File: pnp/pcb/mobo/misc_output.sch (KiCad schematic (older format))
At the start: 45 parts, among them J10 MF3, J11 MF4, J12 DOWNWARDS_LIGHT, J13 UPWARDS_LIGHT, J14 5V_INJECTION, J16 RS-485_2, J17 RS-485_3, J21 AUX1, J22 AUX2, J23 QWIIC1, J24 QWIIC2, J25 RS-485_1, J6 SERVO1, J7 SERVO2, J8 MF1, J9 MF2, Q1 IRF540N, Q2 IRF540N, Q3 IRF540N, Q4 IRF540N, U15 TC4424A, U16 TC4424A, U2 SP3485EN, U3 SP3485EN, U4 SP3485EN

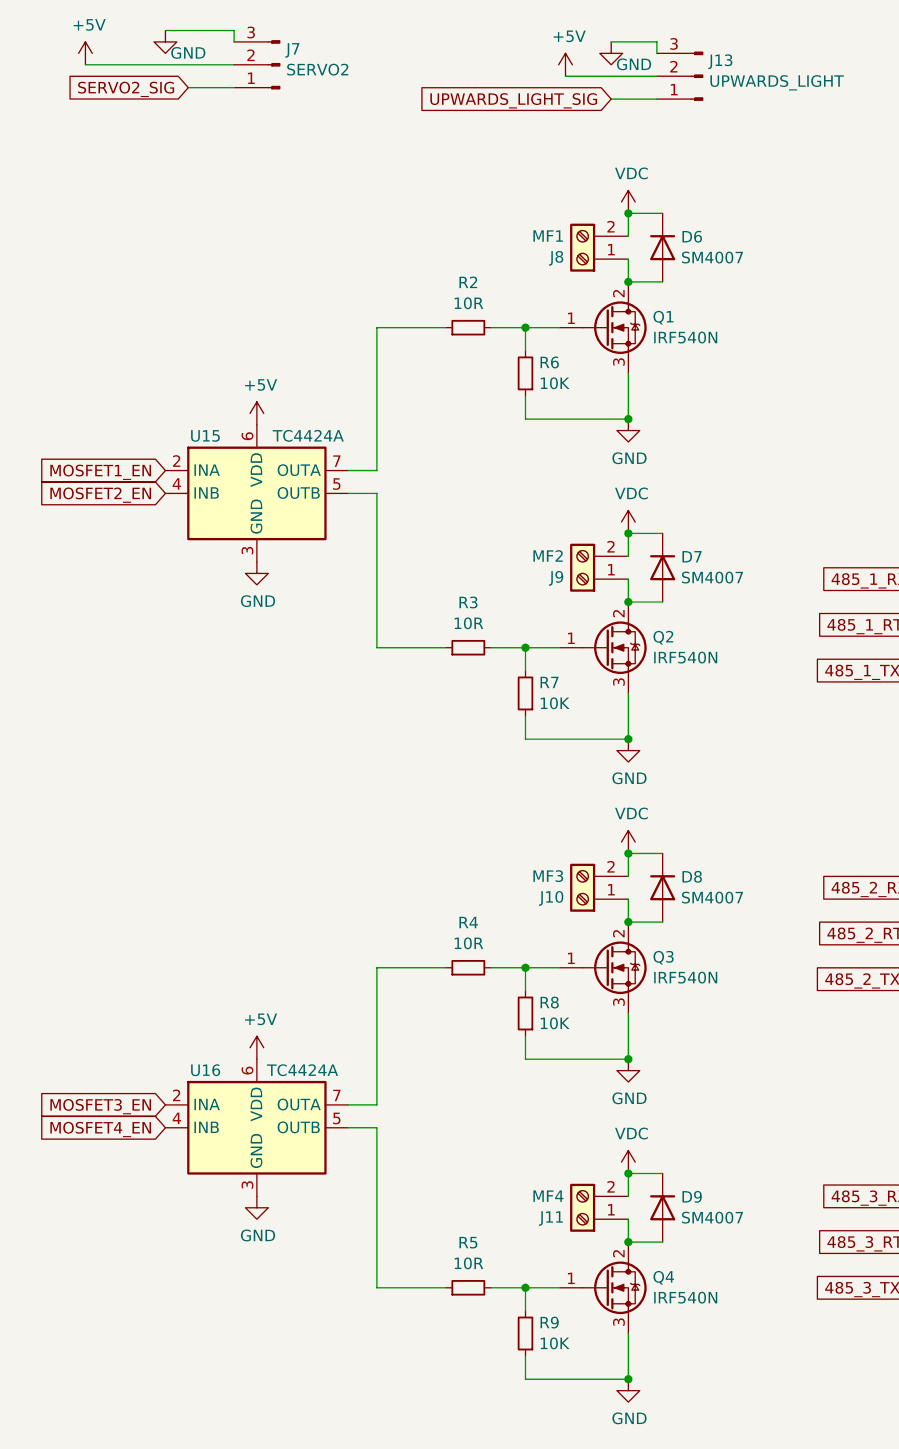
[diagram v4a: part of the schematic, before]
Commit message: Revert 24V support, only routing is left
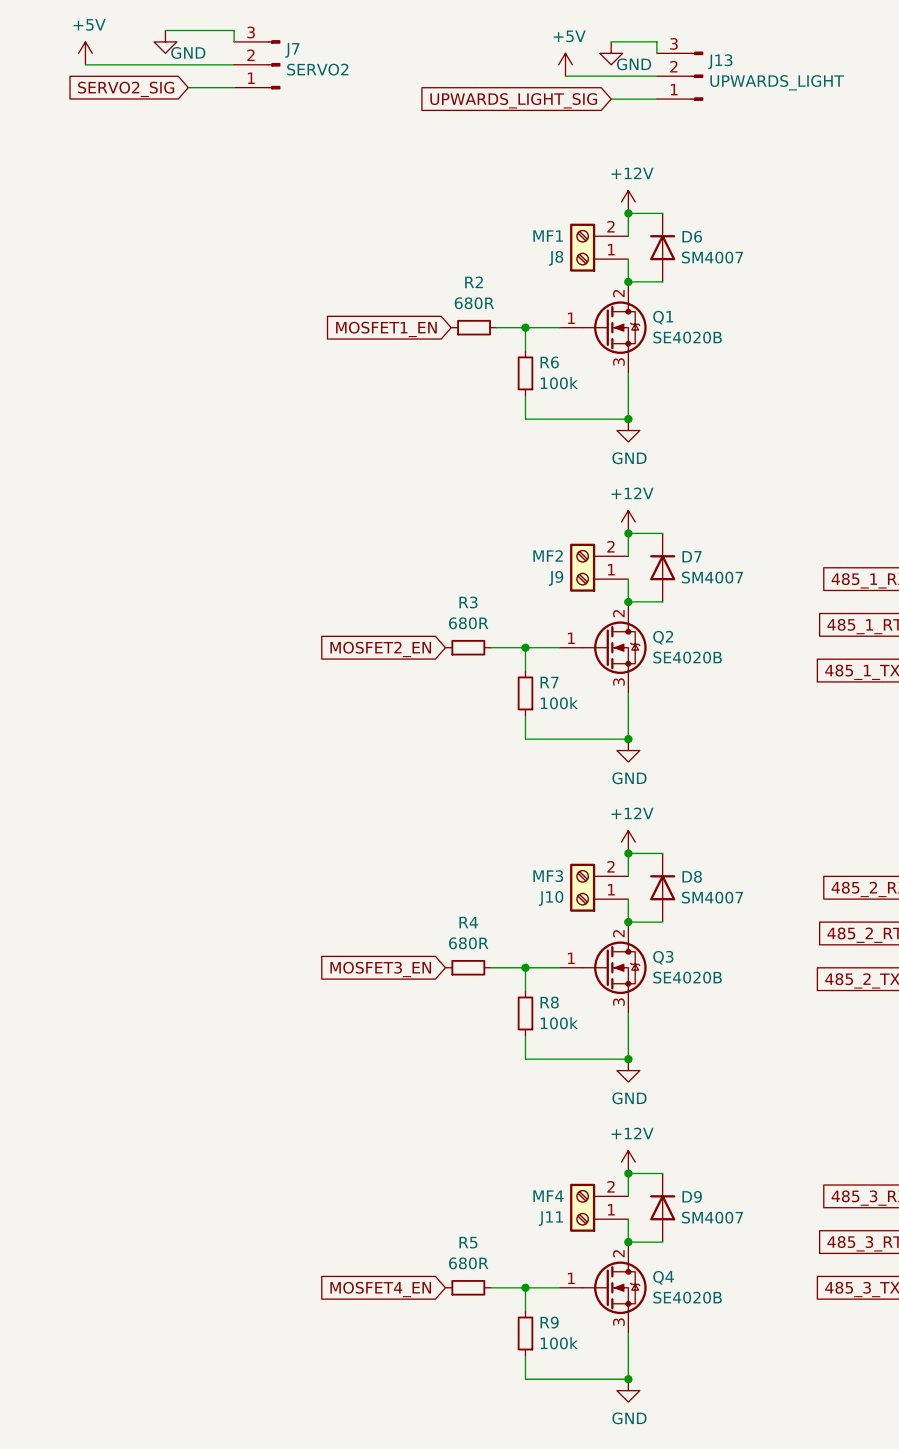
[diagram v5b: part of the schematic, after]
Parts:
- removed Q1, Q2, Q3, Q4: IRF540N, Package_TO_SOT_SMD:TO-252-2, symbol Transistor_FET:IRF540N
- removed U15, U16: TC4424A, Package_SO:SOIC-8_3.9x4.9mm_P1.27mm, symbol index:TC4424A
- added Q1, Q2, Q3, Q4: SE4020B, Package_TO_SOT_SMD:TO-252-2, symbol index:SE4020B
- R2, R3, R4, R5: value 10R -> 680R
- R6, R7, R8, R9: value 10K -> 100k
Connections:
- net GND: now also Q1.3 (S), Q2.3 (S), Q3.3 (S), Q4.3 (S)
- net MOSFET1_EN: now also R2.1
- net MOSFET2_EN: now also R3.1
- net MOSFET3_EN: now also R4.1
- net MOSFET4_EN: now also R5.1
- net at R2.2, R6.2: now also Q1.1 (G)
- net at D6.2 (A), J8.1 (Pin_1): now also Q1.2 (D)
- net at R3.2, R7.2: now also Q2.1 (G)
- net at D7.2 (A), J9.1 (Pin_1): now also Q2.2 (D)
- net at R4.2, R8.2: now also Q3.1 (G)
- net at D8.2 (A), J10.1 (Pin_1): now also Q3.2 (D)
- net at R5.2, R9.2: now also Q4.1 (G)
- net at D9.2 (A), J11.1 (Pin_1): now also Q4.2 (D)
- net VDC renamed +12V
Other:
- moved on the sheet: R2

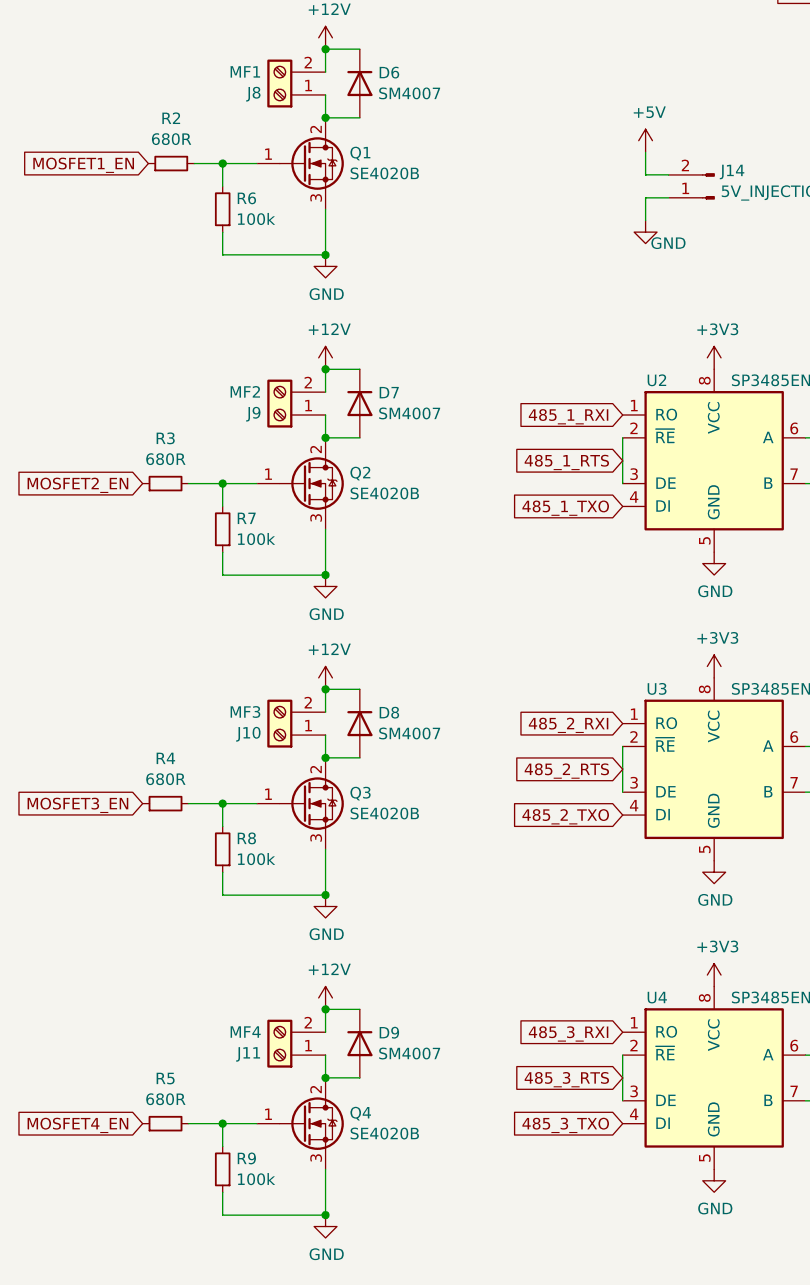
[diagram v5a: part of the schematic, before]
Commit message: Replaced MOSFET with TSM900
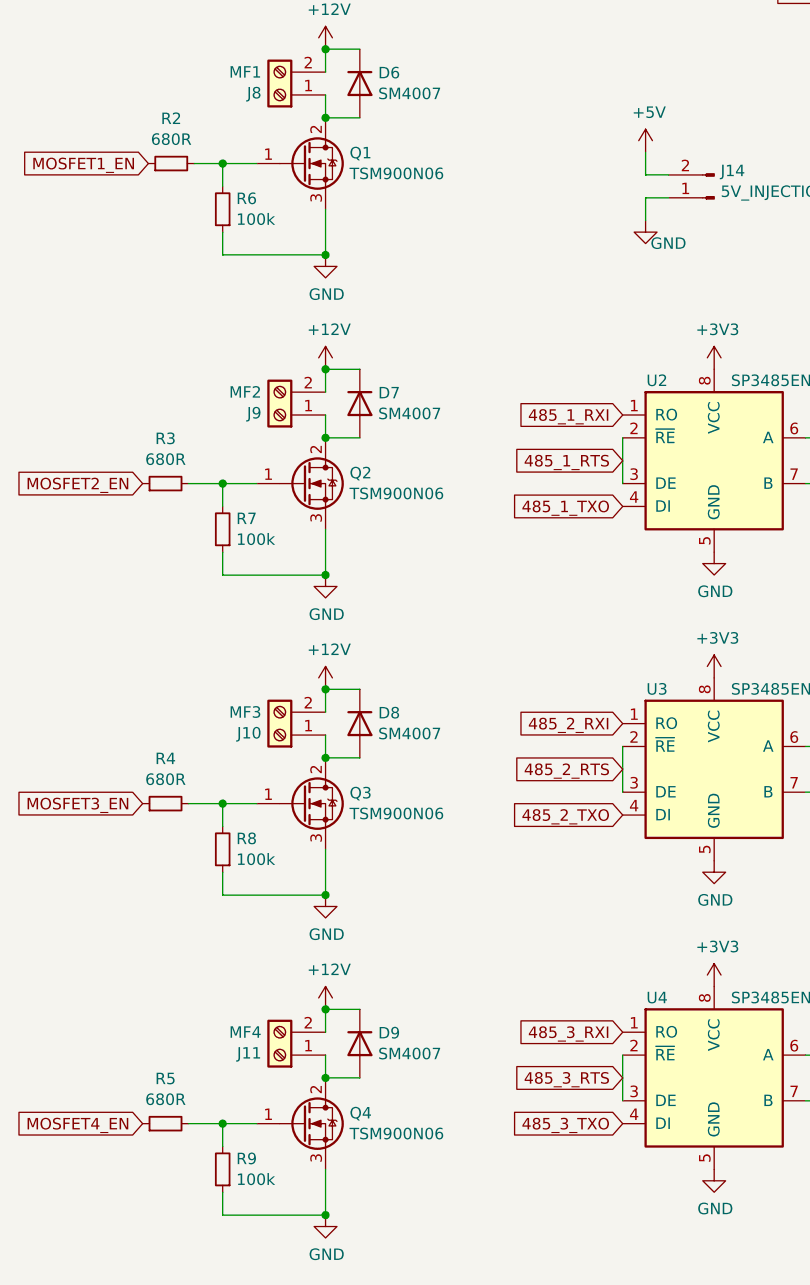
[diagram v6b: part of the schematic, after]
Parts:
- removed Q1, Q2, Q3, Q4: SE4020B, Package_TO_SOT_SMD:TO-252-2, symbol index:SE4020B
- added Q1, Q2, Q3, Q4: TSM900N06, Package_TO_SOT_SMD:TO-252-2, symbol index:TSM900N06
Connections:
- net GND: now also Q1.3 (S), Q2.3 (S), Q3.3 (S), Q4.3 (S)
- net at R2.2, R6.2: now also Q1.1 (G)
- net at D6.2 (A), J8.1 (Pin_1): now also Q1.2 (D)
- net at R3.2, R7.2: now also Q2.1 (G)
- net at D7.2 (A), J9.1 (Pin_1): now also Q2.2 (D)
- net at R4.2, R8.2: now also Q3.1 (G)
- net at D8.2 (A), J10.1 (Pin_1): now also Q3.2 (D)
- net at R5.2, R9.2: now also Q4.1 (G)
- net at D9.2 (A), J11.1 (Pin_1): now also Q4.2 (D)
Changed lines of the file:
@@
 Wire Wire Line
 	2875 2650 3025 2650
-$Comp
-L index:SE4020B Q1
-U 1 1 5FEBE1D6
-P 3225 2650
-F 0 "Q1" H 3430 2696 50  0000 L CNN
-F 1 "SE4020B" H 3430 2605 50  0000 L CNN
-F 2 "Package_TO_SOT_SMD:TO-252-2" H 3475 2575 50  0001 L CIN
-F 3 "https://datasheet.lcsc.com/szlcsc/1912111437_SINO-IC-SE4020B_C396085.pdf" H 3225 2650 50  0001 L CNN
-	1    3225 2650
-	1    0    0    -1
-$EndComp
-Connection ~ 3325 2450
-$Comp
-L index:SE4020B Q2
-U 1 1 5FEC32EF
-P 3225 4050
-F 0 "Q2" H 3430 4096 50  0000 L CNN
-F 1 "SE4020B" H 3430 4005 50  0000 L CNN
-F 2 "Package_TO_SOT_SMD:TO-252-2" H 3475 3975 50  0001 L CIN
-F 3 "https://datasheet.lcsc.com/szlcsc/1912111437_SINO-IC-SE4020B_C396085.pdf" H 3225 4050 50  0001 L CNN
-	1    3225 4050
-	1    0    0    -1
-$EndComp
-Connection ~ 3325 3850
-$Comp
-L index:SE4020B Q3
-U 1 1 5FEC4E58
-P 3225 5450
-F 0 "Q3" H 3430 5496 50  0000 L CNN
-F 1 "SE4020B" H 3430 5405 50  0000 L CNN
-F 2 "Package_TO_SOT_SMD:TO-252-2" H 3475 5375 50  0001 L CIN
-F 3 "https://datasheet.lcsc.com/szlcsc/1912111437_SINO-IC-SE4020B_C396085.pdf" H 3225 5450 50  0001 L CNN
-	1    3225 5450
-	1    0    0    -1
-$EndComp
-Connection ~ 3325 5250
-$Comp
-L index:SE4020B Q4
-U 1 1 5FEC7D03
-P 3225 6850
-F 0 "Q4" H 3430 6896 50  0000 L CNN
-F 1 "SE4020B" H 3430 6805 50  0000 L CNN
-F 2 "Package_TO_SOT_SMD:TO-252-2" H 3475 6775 50  0001 L CIN
-F 3 "https://datasheet.lcsc.com/szlcsc/1912111437_SINO-IC-SE4020B_C396085.pdf" H 3225 6850 50  0001 L CNN
-	1    3225 6850
-	1    0    0    -1
-$EndComp
-Connection ~ 3325 6650
 Wire Wire Line
 	3475 2150 3325 2150
@@
 $EndComp
 Connection ~ 3325 6350
+$Comp
+L index:TSM900N06 Q1
+U 1 1 5FE4F23E
+P 3225 2650
+F 0 "Q1" H 3430 2696 50  0000 L CNN
+F 1 "TSM900N06" H 3430 2605 50  0000 L CNN
+F 2 "Package_TO_SOT_SMD:TO-252-2" H 3475 2575 50  0001 L CIN
+F 3 "https://datasheet.lcsc.com/szlcsc/1912111437_SINO-IC-SE4020B_C396085.pdf" H 3225 2650 50  0001 L CNN
+	1    3225 2650
+	1    0    0    -1
+$EndComp
+Connection ~ 3325 2450
+$Comp
+L index:TSM900N06 Q2
+U 1 1 5FE667F0
+P 3225 4050
+F 0 "Q2" H 3430 4096 50  0000 L CNN
+F 1 "TSM900N06" H 3430 4005 50  0000 L CNN
+F 2 "Package_TO_SOT_SMD:TO-252-2" H 3475 3975 50  0001 L CIN
+F 3 "https://datasheet.lcsc.com/szlcsc/1912111437_SINO-IC-SE4020B_C396085.pdf" H 3225 4050 50  0001 L CNN
+	1    3225 4050
+	1    0    0    -1
+$EndComp
+Connection ~ 3325 3850
+$Comp
+L index:TSM900N06 Q3
+U 1 1 5FE6BC8C
+P 3225 5450
+F 0 "Q3" H 3430 5496 50  0000 L CNN
+F 1 "TSM900N06" H 3430 5405 50  0000 L CNN
+F 2 "Package_TO_SOT_SMD:TO-252-2" H 3475 5375 50  0001 L CIN
+F 3 "https://datasheet.lcsc.com/szlcsc/1912111437_SINO-IC-SE4020B_C396085.pdf" H 3225 5450 50  0001 L CNN
+	1    3225 5450
+	1    0    0    -1
+$EndComp
+Connection ~ 3325 5250
+$Comp
+L index:TSM900N06 Q4
+U 1 1 5FE6CB4C
+P 3225 6850
+F 0 "Q4" H 3430 6896 50  0000 L CNN
+F 1 "TSM900N06" H 3430 6805 50  0000 L CNN
+F 2 "Package_TO_SOT_SMD:TO-252-2" H 3475 6775 50  0001 L CIN
+F 3 "https://datasheet.lcsc.com/szlcsc/1912111437_SINO-IC-SE4020B_C396085.pdf" H 3225 6850 50  0001 L CNN
+	1    3225 6850
+	1    0    0    -1
+$EndComp
+Connection ~ 3325 6650
 $EndSCHEMATC

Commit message: Add MOSFET alternatives
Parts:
- Q2: Alternatives (none) -> SE4020B,NCE6050KA
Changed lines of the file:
@@
 F 2 "Package_TO_SOT_SMD:TO-252-2" H 3475 3975 50  0001 L CIN
 F 3 "https://www.taiwansemi.com/assets/uploads/datasheet/TSM900N06_C1612.pdf" H 3225 4050 50  0001 L CNN
+F 4 "SE4020B,NCE6050KA" H 3225 4050 50  0001 C CNN "Alternatives"
 	1    3225 4050
 	1    0    0    -1
